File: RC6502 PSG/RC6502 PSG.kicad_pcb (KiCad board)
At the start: 2 copper layers, 99.1 x 54.6 mm, 32 parts, among them J1 TRS_3.5mm, J2 Port, J3 Base, J4 RC6502_Backplane, J5 EXT, U1 LM386, U2 74LS373, U3 74LS138, U4 74LS138, U5 SN76489AN, X1 TCXO-14

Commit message: Updated gerbers for order
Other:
- board text added: "BASE"
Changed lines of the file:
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@@
     (links 124)
     (no_connects 0)
-    (area 73.66 85.725 184.765001 153.309048)
+    (area 76.124999 88.189999 175.335001 142.950001)
     (thickness 1.6)
-    (drawings 39)
+    (drawings 60)
     (tracks 505)
     (zones 0)
@@
     )
   )
+  (gr_line (start 113.665 90.805) (end 116.205 90.805) (angle 90) (layer B.SilkS) (width 0.2))
+  (gr_line (start 111.76 88.9) (end 111.76 92.71) (angle 90) (layer B.SilkS) (width 0.2))
+  (gr_line (start 118.11 88.9) (end 111.76 88.9) (angle 90) (layer B.SilkS) (width 0.2))
+  (gr_line (start 118.11 92.71) (end 118.11 88.9) (angle 90) (layer B.SilkS) (width 0.2))
+  (gr_line (start 111.76 92.71) (end 118.11 92.71) (angle 90) (layer B.SilkS) (width 0.2))
+  (gr_line (start 130.81 126.365) (end 150.495 126.365) (angle 90) (layer B.SilkS) (width 0.2))
+  (gr_text READ (at 131.445 131.445 90) (layer B.SilkS)
+    (effects (font (size 1 1) (thickness 0.25)) (justify mirror))
+  )
+  (gr_text WRITE (at 131.445 121.285 90) (layer B.SilkS)
+    (effects (font (size 1 1) (thickness 0.25)) (justify mirror))
+  )
+  (gr_text BASE (at 153.035 126.365 90) (layer B.SilkS)
+    (effects (font (size 1 1) (thickness 0.25)) (justify mirror))
+  )
+  (gr_line (start 150.495 116.205) (end 130.175 116.205) (angle 90) (layer B.SilkS) (width 0.2))
+  (gr_line (start 150.495 136.525) (end 130.175 136.525) (angle 90) (layer B.SilkS) (width 0.2))
+  (gr_line (start 171.45 136.525) (end 151.13 136.525) (angle 90) (layer B.SilkS) (width 0.2))
+  (gr_line (start 171.45 116.205) (end 171.45 136.525) (angle 90) (layer B.SilkS) (width 0.2))
+  (gr_line (start 151.13 116.205) (end 171.45 116.205) (angle 90) (layer B.SilkS) (width 0.2))
+  (gr_line (start 151.13 136.525) (end 151.13 116.205) (angle 90) (layer B.SilkS) (width 0.2))
+  (gr_line (start 150.495 116.205) (end 150.495 136.525) (angle 90) (layer B.SilkS) (width 0.2))
+  (gr_line (start 130.175 136.525) (end 130.175 116.205) (angle 90) (layer B.SilkS) (width 0.2))
+  (gr_line (start 171.45 116.205) (end 171.45 136.525) (angle 90) (layer B.SilkS) (width 0.2))
+  (gr_line (start 146.685 130.175) (end 149.225 130.175) (angle 90) (layer B.SilkS) (width 0.2))
+  (gr_line (start 146.685 120.015) (end 149.225 120.015) (angle 90) (layer B.SilkS) (width 0.2))
+  (gr_line (start 167.64 122.555) (end 170.18 122.555) (angle 90) (layer B.SilkS) (width 0.2))
   (gr_text $xC00 (at 138.43 135.255) (layer B.SilkS)
     (effects (font (size 0.8 0.8) (thickness 0.1)) (justify mirror))
@@
     (effects (font (size 1 1) (thickness 0.25)))
   )
-  (gr_text https://hvetebolle.blogspot.com (at 111.76 105.41) (layer B.SilkS)
+  (gr_text https://hvetebolle.blogspot.com (at 77.47 114.935 90) (layer B.SilkS)
     (effects (font (size 1.5 1.5) (thickness 0.3)) (justify mirror))
   )
@@
   (segment (start 116.332 112.228) (end 116.292 112.268) (width 0.25) (layer B.Cu) (net 4))
   (segment (start 144.145 104.775) (end 147.32 104.775) (width 0.25) (layer F.Cu) (net 5))
-  (segment (start 139.065 109.22) (end 142.24 109.22) (width 0.25) (layer F.Cu) (net 6) (status C00000))
-  (segment (start 134.065 109.22) (end 134.065 108.665) (width 0.25) (layer F.Cu) (net 7) (status C00000))
-  (segment (start 134.065 108.665) (end 133.35 107.95) (width 0.25) (layer F.Cu) (net 7) (status 400000))
+  (segment (start 139.065 109.22) (end 142.24 109.22) (width 0.25) (layer F.Cu) (net 6))
+  (segment (start 134.065 109.22) (end 134.065 108.665) (width 0.25) (layer F.Cu) (net 7))
+  (segment (start 134.065 108.665) (end 133.35 107.95) (width 0.25) (layer F.Cu) (net 7))
   (segment (start 134.192 107.108) (end 133.985 107.315) (width 0.25) (layer F.Cu) (net 7))
   (segment (start 133.985 107.315) (end 134.62 106.68) (width 0.25) (layer F.Cu) (net 7))

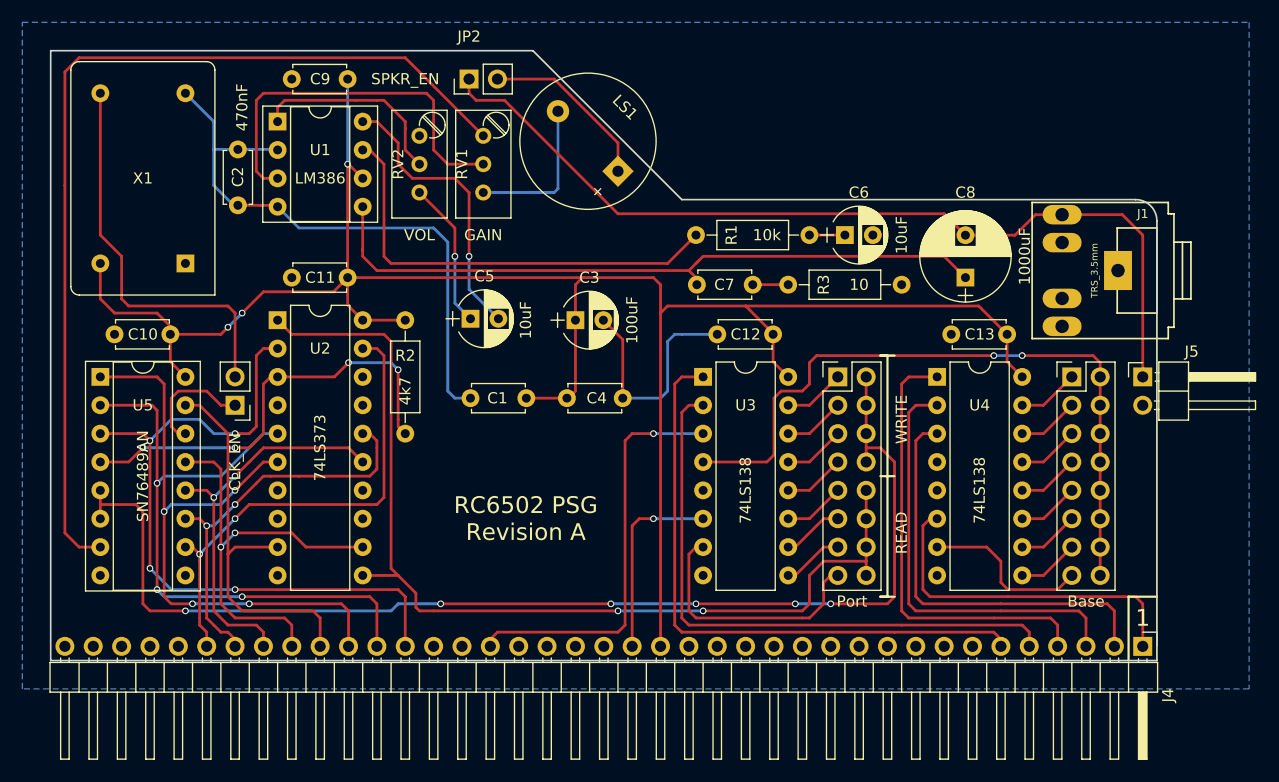
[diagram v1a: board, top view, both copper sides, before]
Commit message: Revised PSG module
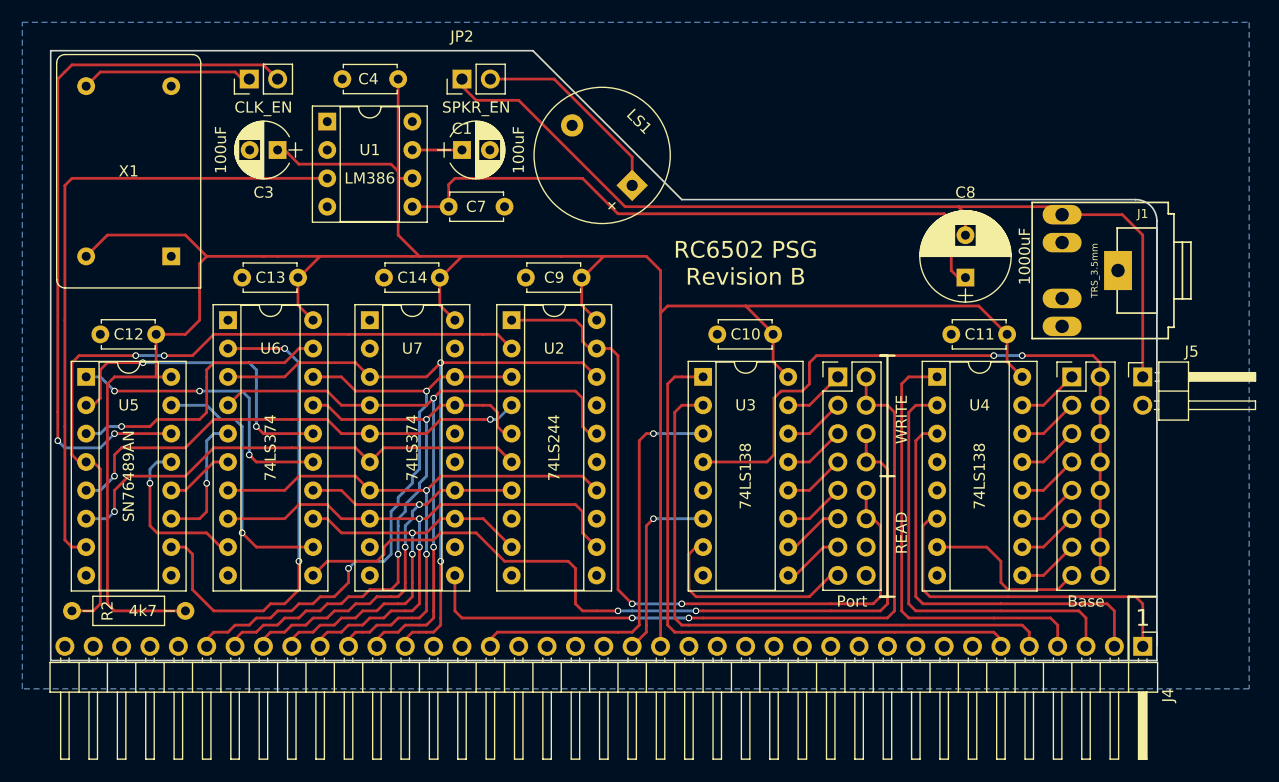
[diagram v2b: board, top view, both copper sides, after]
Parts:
- removed C2: 470nF, Capacitors_THT:C_Disc_D4.7mm_W2.5mm_P5.00mm
- removed C5, C6: 10uF, Capacitors_THT:CP_Radial_D5.0mm_P2.50mm
- removed R1: 10k, Resistors_THT:R_Axial_DIN0207_L6.3mm_D2.5mm_P10.16mm_Horizontal
- removed R3: 10, Resistors_THT:R_Axial_DIN0207_L6.3mm_D2.5mm_P10.16mm_Horizontal
- removed RV1, RV2: 10K, Potentiometers:Potentiometer_Trimmer_Bourns_3296W
- added C14: 100nF, Capacitors_THT:C_Disc_D4.7mm_W2.5mm_P5.00mm, F.Cu at (106.0, 108.6)
- added U6: 74LS374, Housings_DIP:DIP-20_W7.62mm_Socket, F.Cu at (92.1, 112.4)
- added U7: 74LS374, Housings_DIP:DIP-20_W7.62mm_Socket, F.Cu at (104.8, 112.4)
- C1: value 100nF -> 100uF; footprint Capacitors_THT:C_Disc_D4.7mm_W2.5mm_P5.00mm -> Capacitors_THT:CP_Radial_D5.0mm_P2.50mm
- U2: value 74LS373 -> 74LS244; footprint Housings_DIP:DIP-20_W7.62mm -> Housings_DIP:DIP-20_W7.62mm_Socket
- U3, U4: footprint Housings_DIP:DIP-16_W7.62mm -> Housings_DIP:DIP-16_W7.62mm_Socket
- moved C13 63.7 mm to (93.3, 108.6)
- moved C11 59.3 mm to (156.8, 113.7)
- moved C12 55.2 mm to (80.6, 113.7)
- moved C10 54.0 mm to (135.9, 113.7)
- moved R2 32.6 mm to (88.3, 138.4), turned to 180 degrees
- moved C4 32.3 mm to (107.3, 90.8), turned to 180 degrees
- moved C3 30.7 mm to (96.5, 97.2), turned to 180 degrees
- moved JP1 29.2 mm to (94.0, 90.8), turned to 90 degrees
- moved C9 27.5 mm to (118.7, 108.6)
- moved C7 23.3 mm to (116.8, 102.2)
- moved C1 22.2 mm to (113.0, 97.2)
- moved U2 21.0 mm to (117.5, 112.4)
- moved U1 4.45 mm to (101.0, 94.6)
- moved LS1 1.80 mm to (128.3, 100.3)
- moved X1 1.42 mm to (87.0, 106.7)
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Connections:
- C1 pad 1: GND -> Net-(C1-Pad1)
- C1 pad 2: VCC -> GND
- C7 pad 1: Net-(C7-Pad1) -> GND
- J2 pad 14: READ -> (no net)
- J2 pad 16: READ -> (no net)
- J2 pad 2: WRITE -> WR_SIGNAL
- J2 pad 4: WRITE -> WR_SIGNAL
- J2 pad 6: WRITE -> WR_DATA
- J2 pad 8: WRITE -> WR_DATA
- JP1 pad 1: /CLK -> Net-(JP1-Pad1)
- JP1 pad 2: Net-(JP1-Pad2) -> /CLK
- R2 pad 2: READY -> /S_RDY
- U1 pad 1: Net-(RV2-Pad2) -> (no net)
- U1 pad 3: Net-(RV1-Pad2) -> Line
- U1 pad 7: Net-(R1-Pad1) -> Net-(C1-Pad1)
- U1 pad 8: Net-(C5-Pad2) -> (no net)
- U2 pad 11: READ -> GND
- U2 pad 12: /D4 -> /D3
- U2 pad 14: GND -> /D2
- U2 pad 15: /D5 -> GND
- U2 pad 16: /D6 -> /D1
- U2 pad 18: GND -> /D0
- U2 pad 19: /D7 -> READ
- U2 pad 2: /D0 -> /S_RDY
- U2 pad 3: READY -> /D7
- U2 pad 4: GND -> /S_WE
- U2 pad 5: /D1 -> /D6
- U2 pad 6: /D2 -> /S_CE
- U2 pad 7: GND -> /D5
- U2 pad 9: /D3 -> /D4
- U5 pad 1: /D2 -> /S_D2
- U5 pad 10: /D7 -> /S_D7
- U5 pad 11: /D6 -> /S_D6
- U5 pad 12: /D5 -> /S_D5
- U5 pad 13: /D4 -> /S_D4
- U5 pad 15: /D3 -> /S_D3
- U5 pad 2: /D1 -> /S_D1
- U5 pad 3: /D0 -> /S_D0
- U5 pad 4: READY -> /S_RDY
- U5 pad 5: WRITE -> /S_WE
- U5 pad 6: WRITE -> /S_CE
- X1 pad 8: Net-(JP1-Pad2) -> Net-(JP1-Pad1)
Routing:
- net WRITE: track 105.7 -> 0.00 mm, vias 6 -> 0
- net GND: track 88.7 -> 0.00 mm
- net WR_DATA: track 0.00 -> 75.8 mm, vias 0 -> 2
- net /S_RDY: track 0.00 -> 67.1 mm, vias 0 -> 2
- net WR_SIGNAL: track 0.00 -> 66.2 mm, vias 0 -> 2
- net /CLK: track 10.6 -> 63.8 mm, vias 0 -> 2
- net VCC: track 182.0 -> 230.9 mm, vias 3 -> 0
- net /S_D7: track 0.00 -> 43.6 mm, vias 0 -> 2
- net /S_WE: track 0.00 -> 43.4 mm, vias 0 -> 2
- net /S_CE: track 0.00 -> 43.4 mm, vias 0 -> 1
- net Net-(R1-Pad1): track 39.9 -> 0.00 mm
- net READY: track 39.2 -> 0.00 mm, vias 4 -> 0
- net Net-(JP1-Pad2): track 35.6 -> 0.00 mm
- net Net-(RV1-Pad2): track 34.3 -> 0.00 mm
- net /S_D1: track 0.00 -> 29.0 mm, vias 0 -> 2
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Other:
- board text added: "RC6502 PSG Revision B"
- board text removed: "GAIN"
- board text removed: "RC6502 PSG Revision A"
- board text removed: "VOL"
